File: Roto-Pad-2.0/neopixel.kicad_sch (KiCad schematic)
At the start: 30 parts

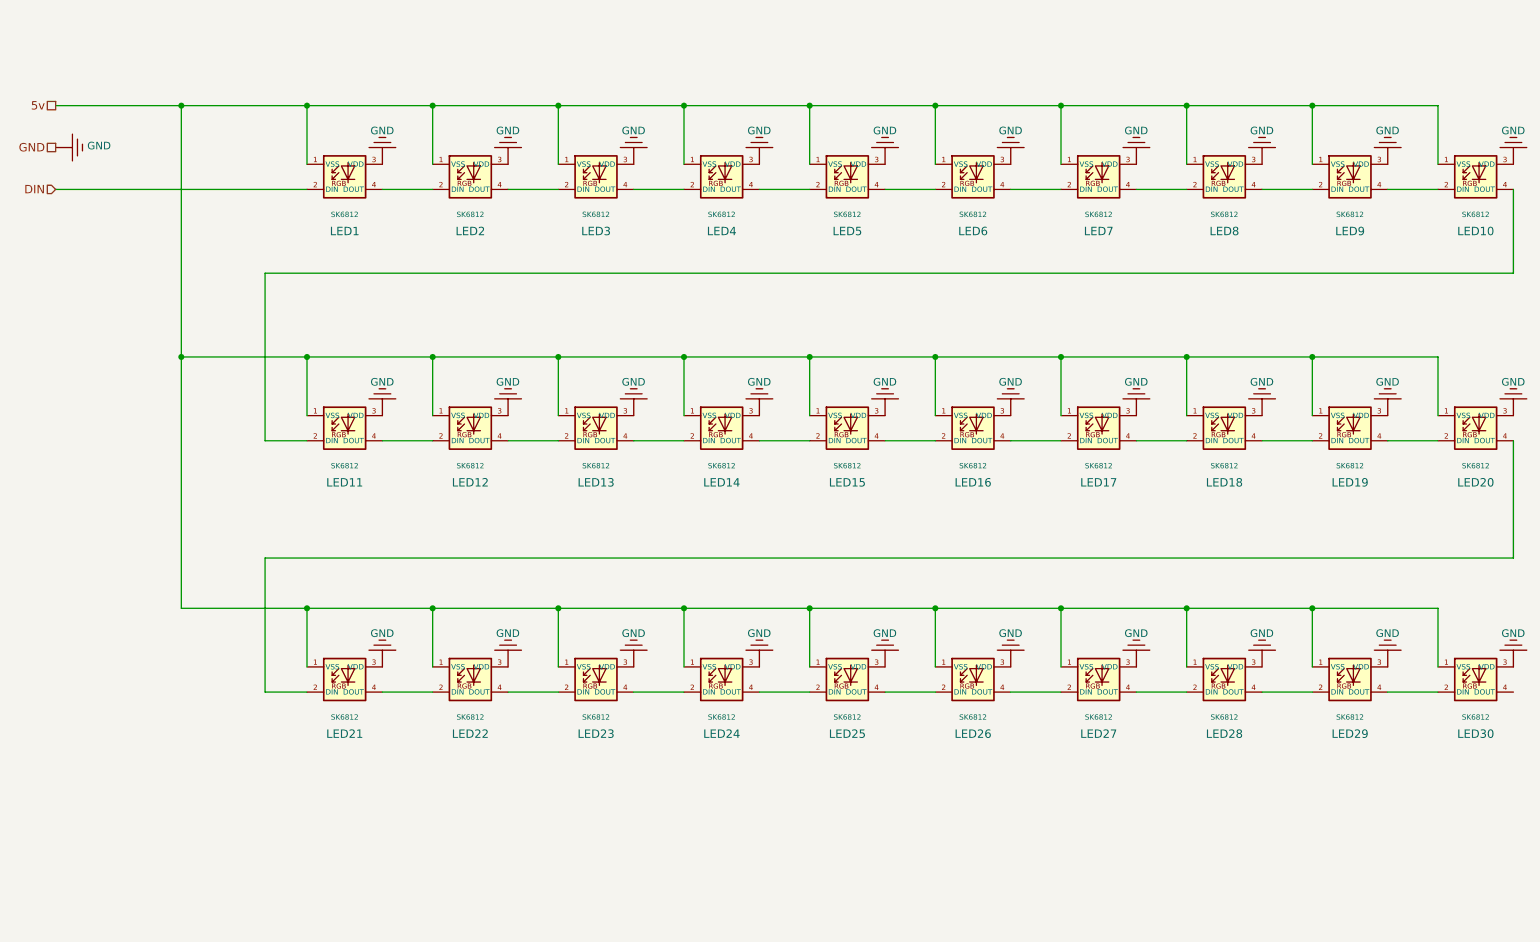
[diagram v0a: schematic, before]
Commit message: completed schematic, passes ERC
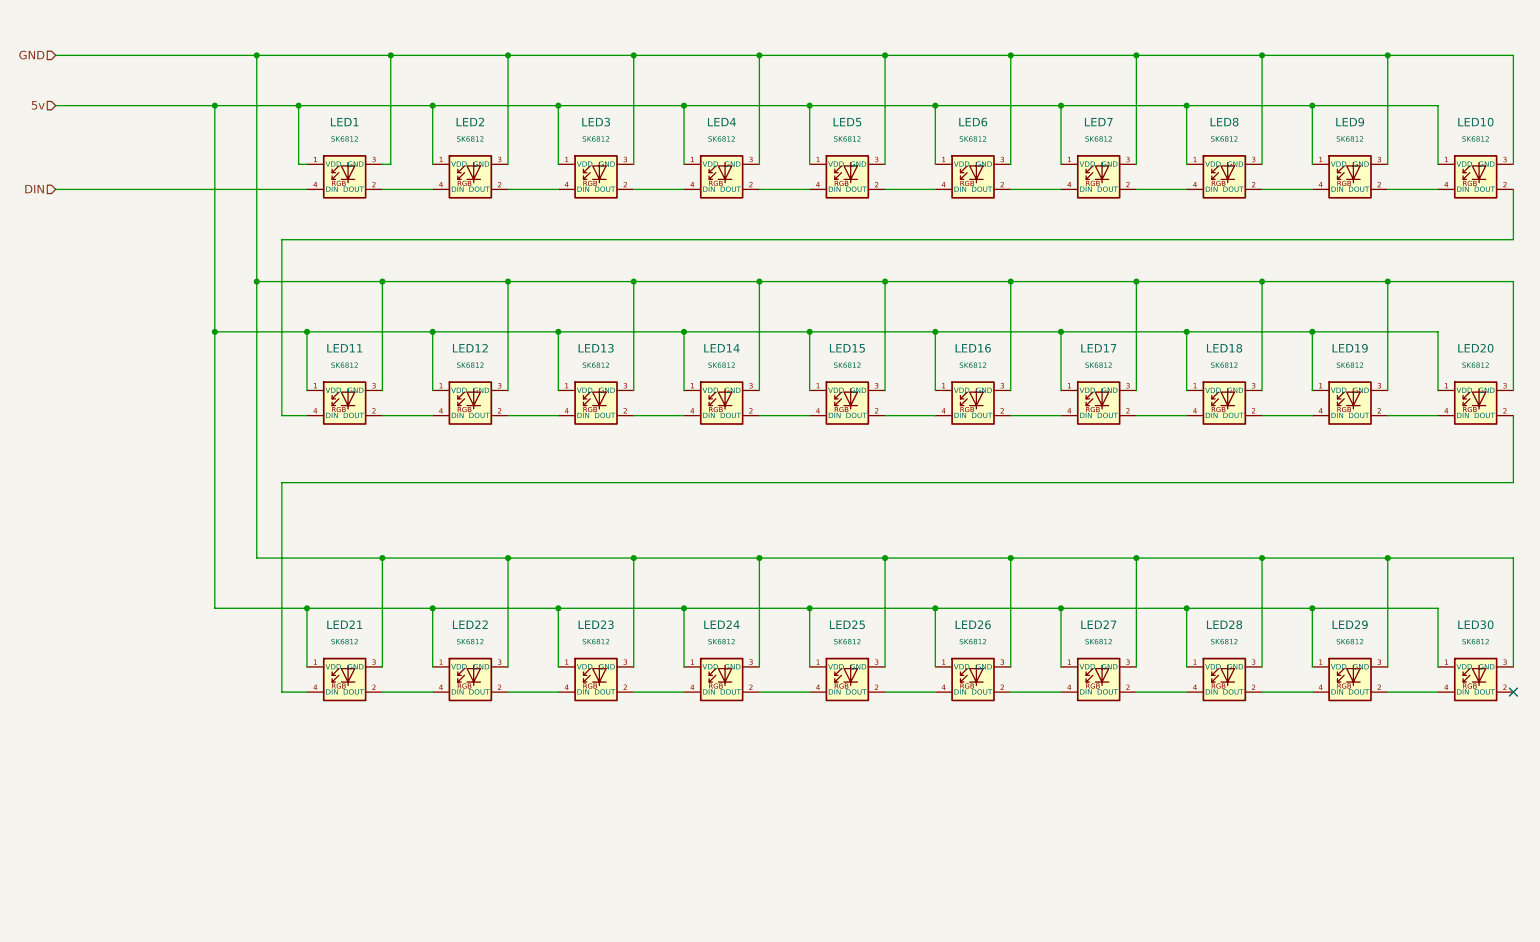
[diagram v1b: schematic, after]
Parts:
- LED1, LED10, LED11, LED12, LED13, LED14, LED15, LED16, LED17, LED18, LED19, LED2, LED20, LED21, LED22, LED23, LED24, LED25, LED26, LED27, LED28, LED29, LED3, LED30, LED4, LED5, LED6, LED7, LED8, LED9: footprint Keebio-Parts:SK6812-MINI-E -> Custom:SK6812-Mini-E MX
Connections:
- net DIN: now also LED1.4 (DIN); no longer LED1.2 (DIN)
- net at LED18.4 (DIN): now also LED17.2 (DOUT); no longer LED19.2 (DIN)
- net at LED20.2 (DOUT): now also LED21.4 (DIN); no longer LED19.4 (DOUT)
- net at LED7.4 (DIN): now also LED6.2 (DOUT); no longer LED8.2 (DIN)
- net at LED8.4 (DIN): now also LED7.2 (DOUT); no longer LED9.2 (DIN)
- net at LED24.2 (DOUT): now also LED25.4 (DIN); no longer LED23.4 (DOUT)
- net at LED24.4 (DIN): now also LED23.2 (DOUT); no longer LED25.2 (DIN)
- net at LED10.2 (DOUT): now also LED11.4 (DIN); no longer LED9.4 (DOUT)
- net at LED11.2 (DOUT): now also LED12.4 (DIN); no longer LED10.4 (DOUT)
- net at LED17.4 (DIN): now also LED16.2 (DOUT); no longer LED18.2 (DIN)
- net at LED26.2 (DOUT): now also LED27.4 (DIN); no longer LED25.4 (DOUT)
- net at LED26.4 (DIN): now also LED25.2 (DOUT); no longer LED27.2 (DIN)
- net at LED28.2 (DOUT): now also LED29.4 (DIN); no longer LED27.4 (DOUT)
- net at LED3.2 (DOUT): now also LED4.4 (DIN); no longer LED2.4 (DOUT)
- net at LED4.2 (DOUT): now also LED5.4 (DIN); no longer LED3.4 (DOUT)
- net at LED12.2 (DOUT): now also LED13.4 (DIN); no longer LED11.4 (DOUT)
- net at LED15.2 (DOUT): now also LED16.4 (DIN); no longer LED14.4 (DOUT)
- net at LED15.4 (DIN): now also LED14.2 (DOUT); no longer LED16.2 (DIN)
- net at LED6.4 (DIN): now also LED5.2 (DOUT); no longer LED7.2 (DIN)
- net at LED20.4 (DIN): now also LED19.2 (DOUT); no longer LED21.2 (DIN)
- net at LED22.2 (DOUT): now also LED23.4 (DIN); no longer LED21.4 (DOUT)
- net at LED22.4 (DIN): now also LED21.2 (DOUT); no longer LED23.2 (DIN)
- net at LED28.4 (DIN): now also LED27.2 (DOUT); no longer LED29.2 (DIN)
- net at LED30.2 (DOUT): no longer LED29.4 (DOUT)
- net at LED30.4 (DIN): now also LED29.2 (DOUT)
- net at LED2.2 (DOUT): now also LED3.4 (DIN); no longer LED1.4 (DOUT)
- net at LED13.2 (DOUT): now also LED14.4 (DIN); no longer LED12.4 (DOUT)
- new net: LED1.2 (DOUT), LED2.4 (DIN)
- new net: LED10.4 (DIN), LED9.2 (DOUT)
- new net: LED8.2 (DOUT), LED9.4 (DIN)
- new net: LED18.2 (DOUT), LED19.4 (DIN)
- no-connect marks 0 -> 1

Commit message: added more heirarchical sheets, debouncing
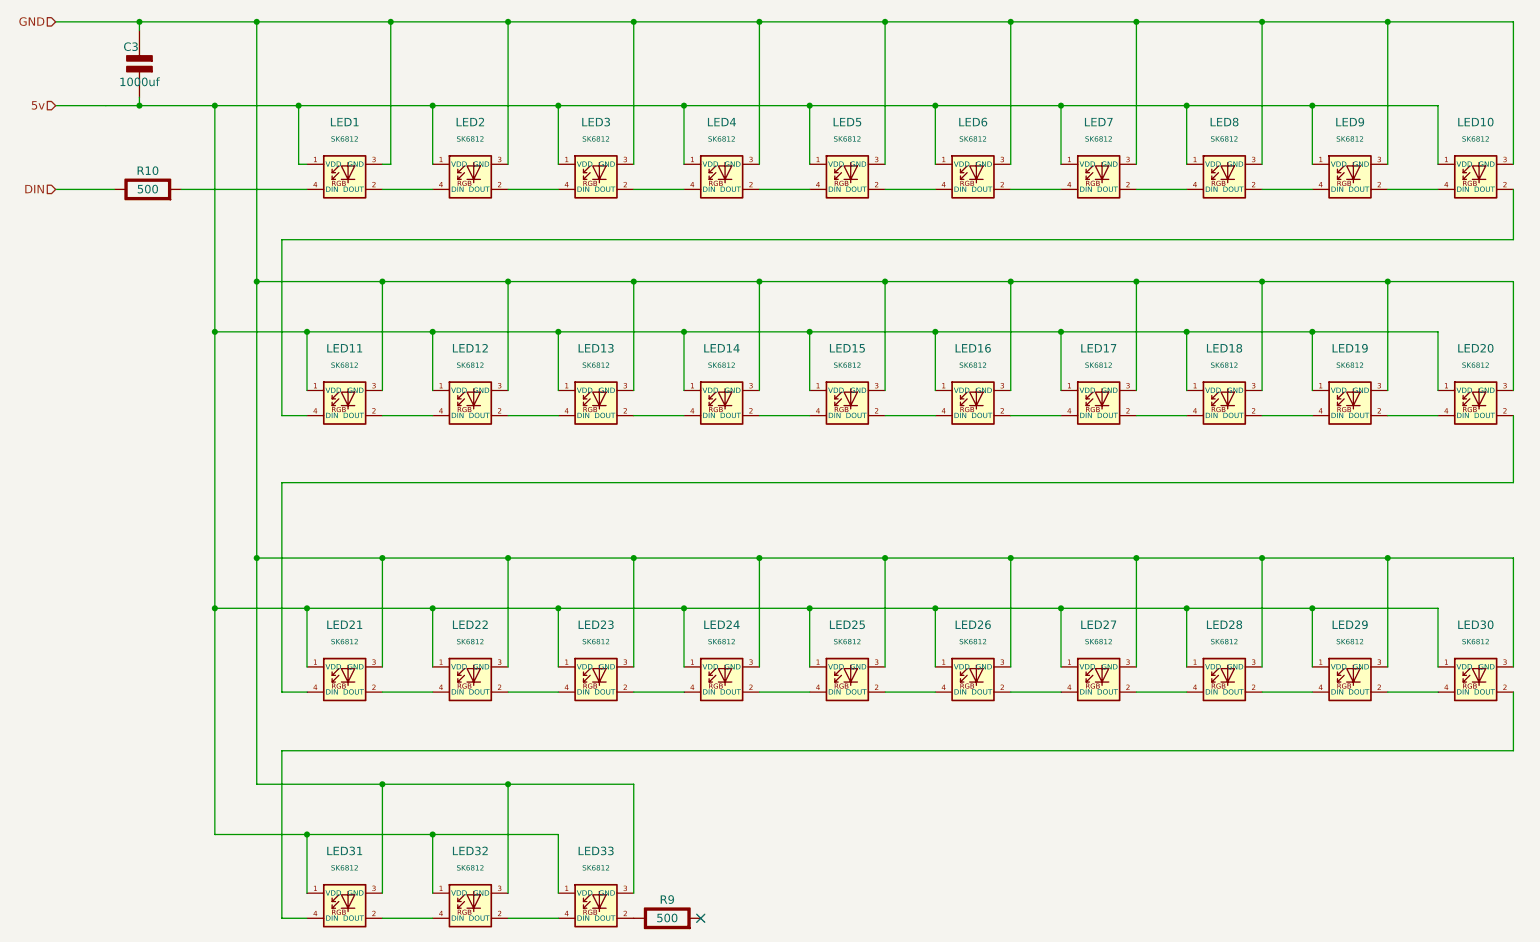
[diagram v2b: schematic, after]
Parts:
- added C3: 1000uf, symbol PCM_Elektuur:C
- added LED31, LED32, LED33: SK6812, Custom:SK6812-Mini-E MX, symbol SparkFun-DiscreteSemi:SK6812
- added R10, R9: 500, symbol PCM_Elektuur:R
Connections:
- net 5v: now also C3.1 (+), LED31.1 (VDD), LED32.1 (VDD), LED33.1 (VDD)
- net DIN: now also R10.1 (+); no longer LED1.4 (DIN)
- net GND: now also C3.2 (-), LED31.3 (GND), LED32.3 (GND), LED33.3 (GND)
- net at LED30.2 (DOUT): now also LED31.4 (DIN)
- new net: LED31.2 (DOUT), LED32.4 (DIN)
- new net: LED32.2 (DOUT), LED33.4 (DIN)
- new net: LED33.2 (DOUT), R9.1 (+)
- new net: LED1.4 (DIN), R10.2 (-)

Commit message: layout completed, first draft of routing
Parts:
- removed C3: 1000uf, symbol PCM_Elektuur:C
- added C1: C-polar 1000uf, Capacitors:NIC_10X10.5_CAP, symbol PCM_Elektuur:C-polar
- added LED34, LED35: SK6812, PCM_LED_SMD_AKL:LED_SK6812_EC15_1.5x1.5mm, symbol SparkFun-DiscreteSemi:SK6812
- LED26, LED27, LED28, LED29, LED30, LED31, LED32, LED33: footprint Custom:SK6812-Mini-E MX -> PCM_LED_SMD_AKL:LED_SK6812_EC15_1.5x1.5mm
- R10, R9: footprint (none) -> adafruit:R1206
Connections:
- net 5v: now also C1.1 (+), LED34.1 (VDD), LED35.1 (VDD)
- net GND: now also C1.2 (-), LED34.3 (GND), LED35.3 (GND)
- net at LED33.2 (DOUT): now also LED34.4 (DIN); no longer R9.1 (+)
- new net: LED34.2 (DOUT), LED35.4 (DIN)
- new net: LED35.2 (DOUT), R9.1 (+)
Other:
- moved on the sheet: R9

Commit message: finished initial routing
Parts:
- removed C1: C-polar 1000uf, Capacitors:NIC_10X10.5_CAP, symbol PCM_Elektuur:C-polar
- added C13, C14, C15, C16, C17, C18, C19, C20, C21, C22, C23, C24, C25, C26, C27, C28, C29, C3, C30, C31, C32, C33, C34, C35, C36, C37, C38, C39, C4, C40, C41, C42, C43, C44: Capacitor, Capacitors:0805, symbol PCM_SL_Devices:Capacitor_NP
- added C2: 47uF, Capacitors:0805, symbol PCM_SL_Devices:Capacitor_NP
- LED26, LED27, LED28, LED29, LED30, LED31, LED32, LED33, LED34, LED35: footprint PCM_LED_SMD_AKL:LED_SK6812_EC15_1.5x1.5mm -> PCM_LED_SMD_AKL:LED_SK6812_PLCC4_5.0x5.0mm_P3.2mm
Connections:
- net 5v: now also C13.1, C14.1, C15.1, C16.1, C17.1, C18.1, C19.1, C2.1, C20.1, C21.1, C22.1, C23.1, C24.1, C25.1, C26.1, C27.1, C28.1, C29.1, C3.1, C30.1, C31.1, C32.1, C33.1, C34.1, C35.1, C36.1, C37.1, C38.1, C39.1, C4.1, C40.1, C41.1, C42.1, C43.1, C44.1
- net GND: now also C13.2, C14.2, C15.2, C16.2, C17.2, C18.2, C19.2, C2.2, C20.2, C21.2, C22.2, C23.2, C24.2, C25.2, C26.2, C27.2, C28.2, C29.2, C3.2, C30.2, C31.2, C32.2, C33.2, C34.2, C35.2, C36.2, C37.2, C38.2, C39.2, C4.2, C40.2, C41.2, C42.2, C43.2, C44.2
